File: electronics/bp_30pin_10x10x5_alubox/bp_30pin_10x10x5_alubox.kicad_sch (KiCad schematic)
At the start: 2 parts

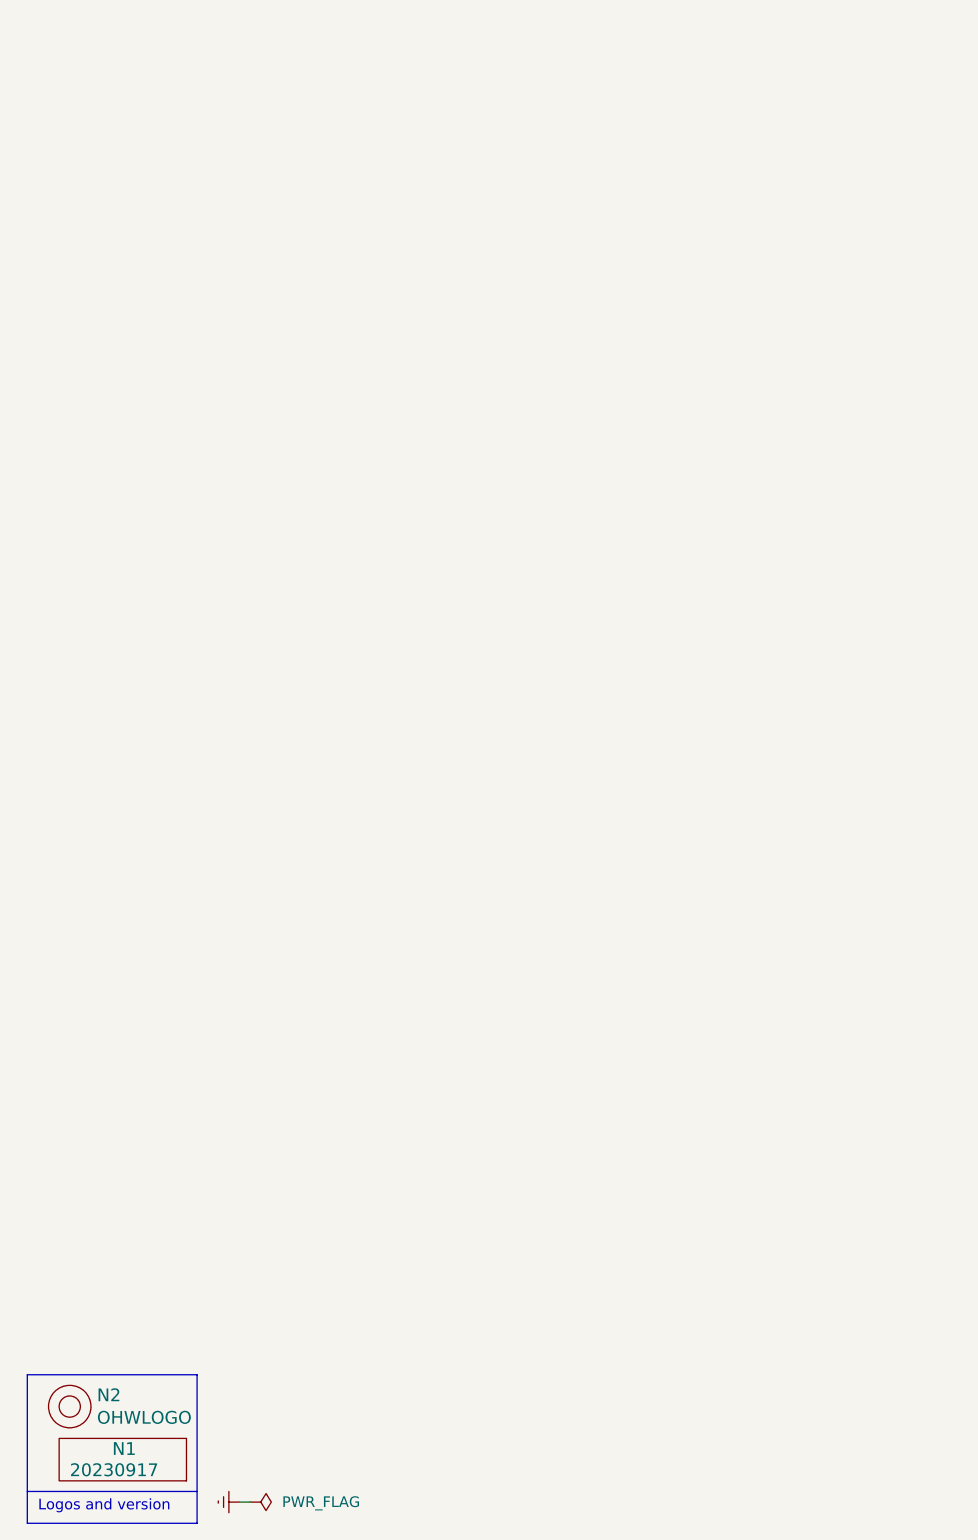
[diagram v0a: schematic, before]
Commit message: added lock files to gitignore, WIP 30 pin backplane
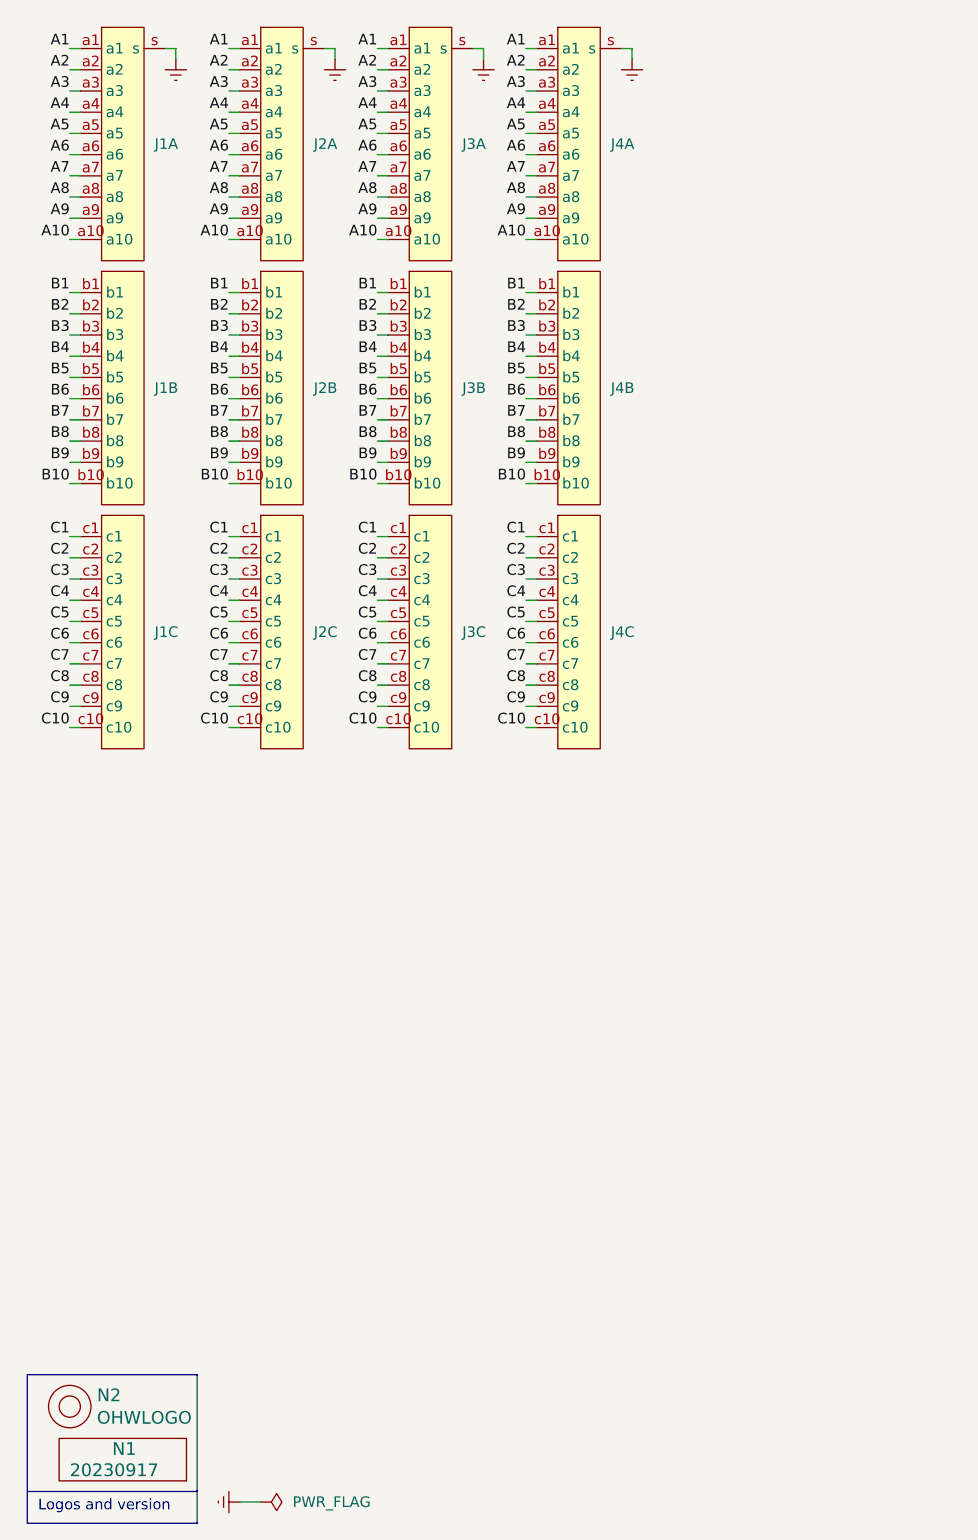
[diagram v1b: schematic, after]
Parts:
- added J1, J2, J3, J4: ~, SquantorConnectors:DIN41612_C3_3x10_Female_Vertical_THT_shields, symbol SquantorConnectors:DIN41612_03x10_ABC_screws
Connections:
- net Earth: now also J1.s, J2.s, J3.s, J4.s
- new net A1: J1.a1, J2.a1, J3.a1, J4.a1
- new net A10: J1.a10, J2.a10, J3.a10, J4.a10
- new net A2: J1.a2, J2.a2, J3.a2, J4.a2
- new net A3: J1.a3, J2.a3, J3.a3, J4.a3
- new net A4: J1.a4, J2.a4, J3.a4, J4.a4
- new net A5: J1.a5, J2.a5, J3.a5, J4.a5
- new net A6: J1.a6, J2.a6, J3.a6, J4.a6
- new net A7: J1.a7, J2.a7, J3.a7, J4.a7
- new net A8: J1.a8, J2.a8, J3.a8, J4.a8
- new net A9: J1.a9, J2.a9, J3.a9, J4.a9
- new net B1: J1.b1, J2.b1, J3.b1, J4.b1
- new net B10: J1.b10, J2.b10, J3.b10, J4.b10
- new net B2: J1.b2, J2.b2, J3.b2, J4.b2
- new net B3: J1.b3, J2.b3, J3.b3, J4.b3
- new net B4: J1.b4, J2.b4, J3.b4, J4.b4
- new net B5: J1.b5, J2.b5, J3.b5, J4.b5
- new net B6: J1.b6, J2.b6, J3.b6, J4.b6
- new net B7: J1.b7, J2.b7, J3.b7, J4.b7
- new net B8: J1.b8, J2.b8, J3.b8, J4.b8
- new net B9: J1.b9, J2.b9, J3.b9, J4.b9
- new net C1: J1.c1, J2.c1, J3.c1, J4.c1
- new net C10: J1.c10, J2.c10, J3.c10, J4.c10
- new net C2: J1.c2, J2.c2, J3.c2, J4.c2
- new net C3: J1.c3, J2.c3, J3.c3, J4.c3
- new net C4: J1.c4, J2.c4, J3.c4, J4.c4
- new net C5: J1.c5, J2.c5, J3.c5, J4.c5
- new net C6: J1.c6, J2.c6, J3.c6, J4.c6
- new net C7: J1.c7, J2.c7, J3.c7, J4.c7
- new net C8: J1.c8, J2.c8, J3.c8, J4.c8
- new net C9: J1.c9, J2.c9, J3.c9, J4.c9

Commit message: Place and route done
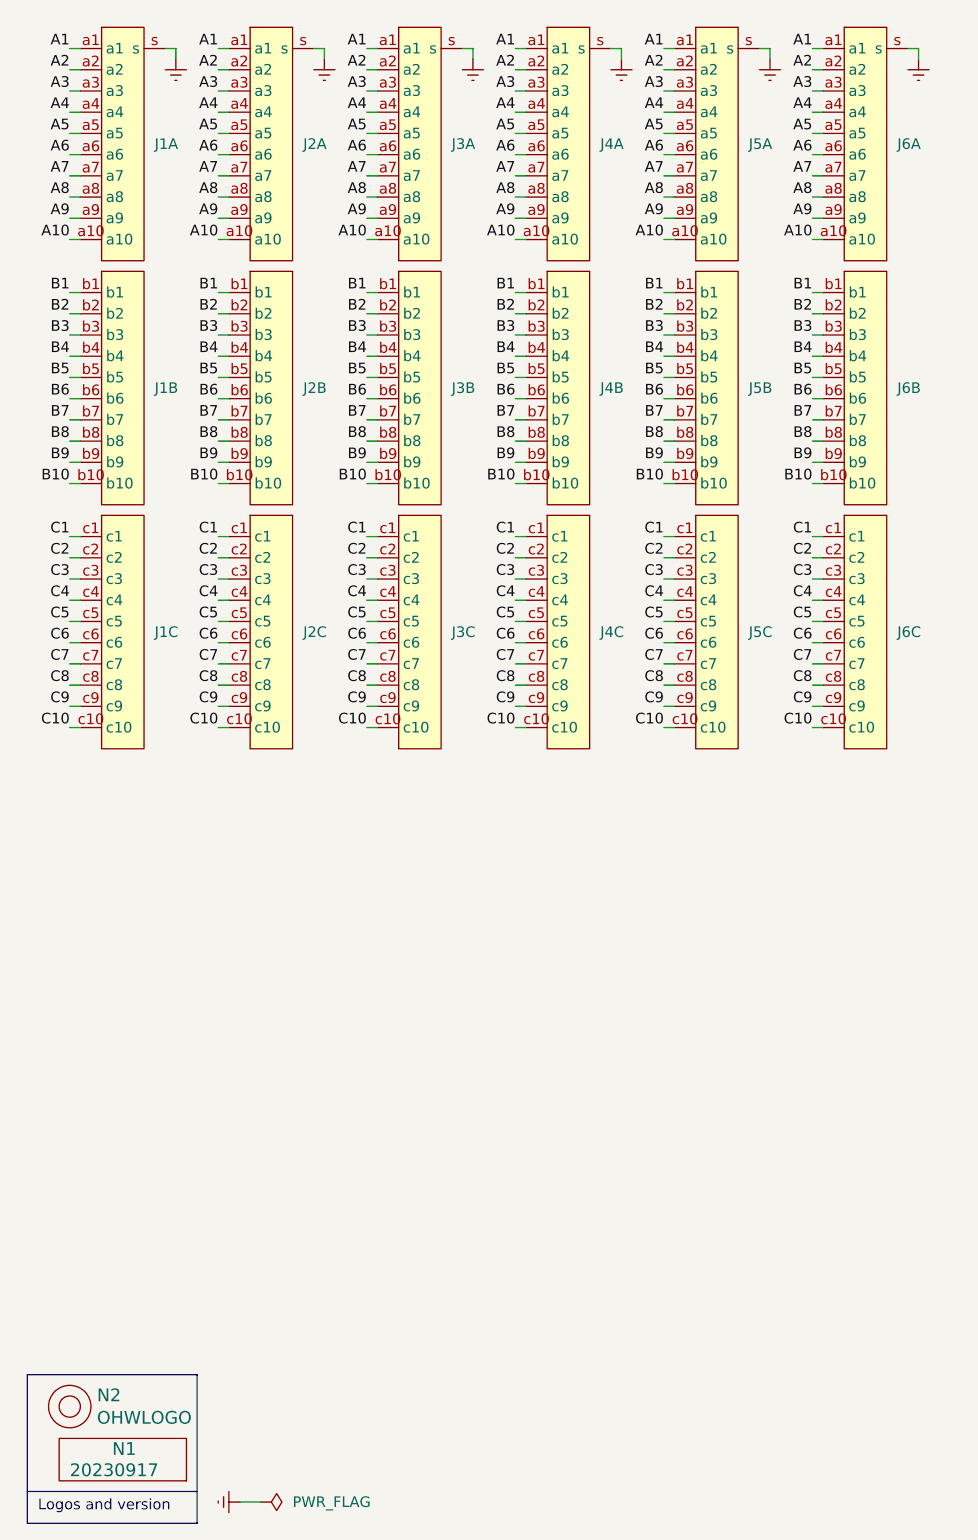
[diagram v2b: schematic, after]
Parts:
- added J5, J6: ~, SquantorConnectors:DIN41612_R3_3x10_Male_Vertical_THT_shield, symbol SquantorConnectors:DIN41612_03x10_ABC_screws
- J1, J2, J3, J4: footprint SquantorConnectors:DIN41612_C3_3x10_Female_Vertical_THT_shields -> SquantorConnectors:DIN41612_R3_3x10_Male_Vertical_THT_shield
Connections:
- net A1: now also J5.a1, J6.a1
- net A10: now also J5.a10, J6.a10
- net A2: now also J5.a2, J6.a2
- net A3: now also J5.a3, J6.a3
- net A4: now also J5.a4, J6.a4
- net A5: now also J5.a5, J6.a5
- net A6: now also J5.a6, J6.a6
- net A7: now also J5.a7, J6.a7
- net A8: now also J5.a8, J6.a8
- net A9: now also J5.a9, J6.a9
- net B1: now also J5.b1, J6.b1
- net B10: now also J5.b10, J6.b10
- net B2: now also J5.b2, J6.b2
- net B3: now also J5.b3, J6.b3
- net B4: now also J5.b4, J6.b4
- net B5: now also J5.b5, J6.b5
- net B6: now also J5.b6, J6.b6
- net B7: now also J5.b7, J6.b7
- net B8: now also J5.b8, J6.b8
- net B9: now also J5.b9, J6.b9
- net C1: now also J5.c1, J6.c1
- net C10: now also J5.c10, J6.c10
- net C2: now also J5.c2, J6.c2
- net C3: now also J5.c3, J6.c3
- net C4: now also J5.c4, J6.c4
- net C5: now also J5.c5, J6.c5
- net C6: now also J5.c6, J6.c6
- net C7: now also J5.c7, J6.c7
- net C8: now also J5.c8, J6.c8
- net C9: now also J5.c9, J6.c9
- net Earth: now also J5.s, J6.s
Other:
- moved on the sheet: J2A, J2B, J2C, J3A, J3B, J3C, J4A, J4B, J4C

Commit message: updated versionnumber, added block for backplane, larger copper plane spacing
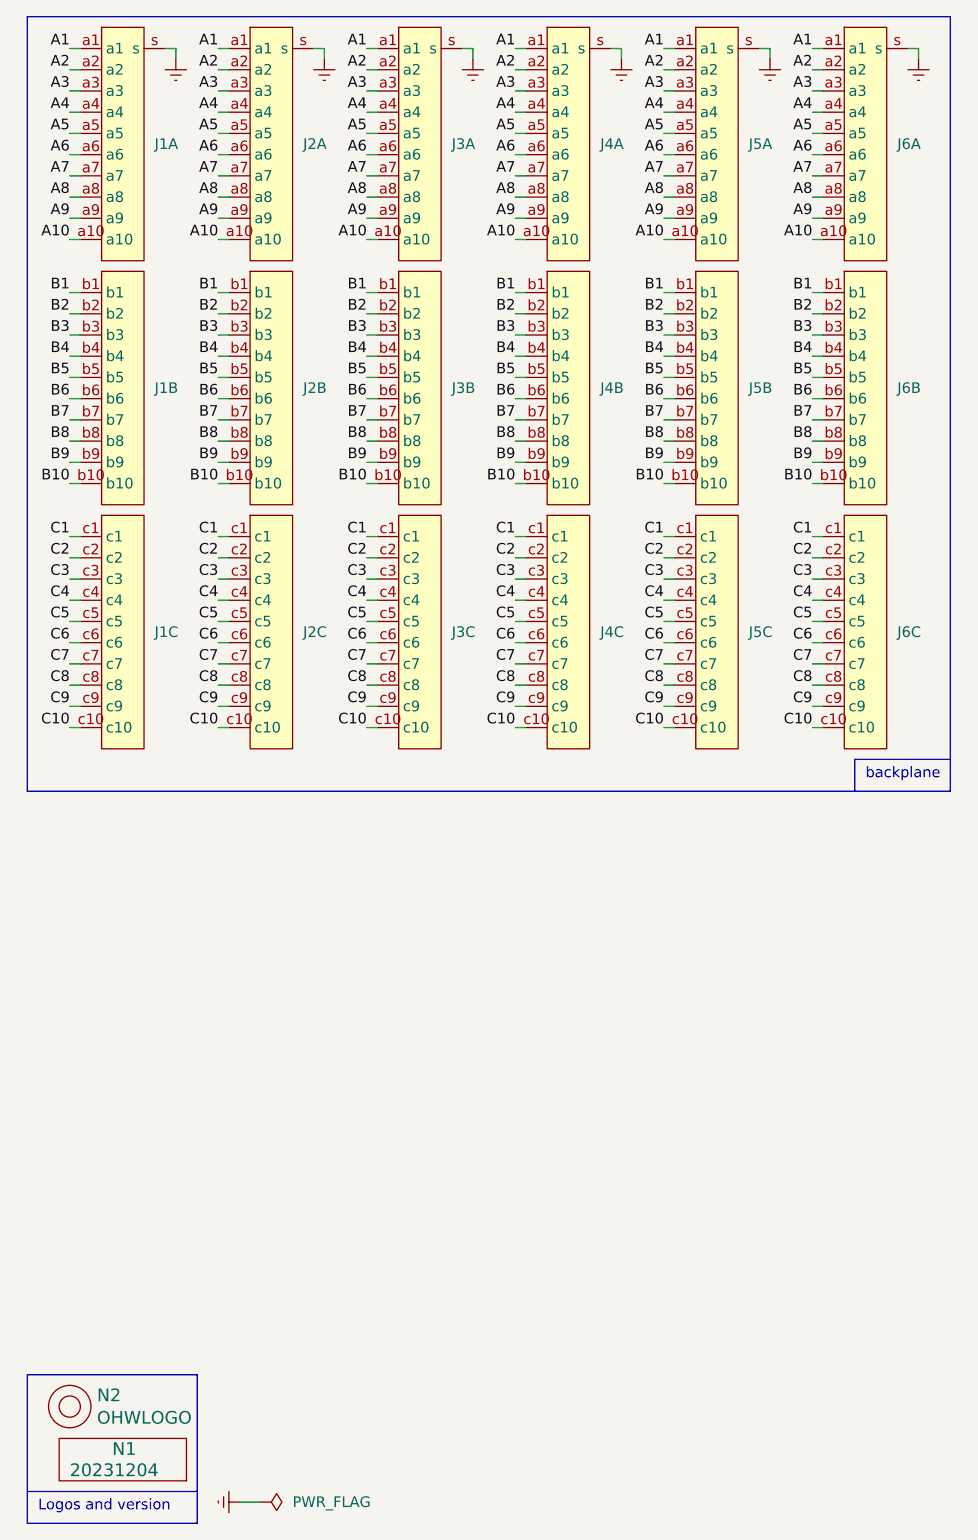
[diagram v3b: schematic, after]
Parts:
- N1: value 20230917 -> 20231204
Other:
- note added: "backplane"
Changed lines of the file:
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@@
+    (stroke (width 0) (type default))
+  )
+  (polyline (pts (xy 15.24 15.24) (xy 125.73 15.24))
     (stroke (width 0) (type default))
   )
@@
     (stroke (width 0) (type default))
   )
+  (polyline (pts (xy 125.73 104.14) (xy 114.3 104.14))
+    (stroke (width 0) (type default))
+  )
   (wire (pts (xy 55.88 66.04) (xy 57.15 66.04))
     (stroke (width 0) (type default))
@@
     (stroke (width 0) (type default))
   )
+  (polyline (pts (xy 114.3 104.14) (xy 114.3 107.95))
+    (stroke (width 0) (type default))
+  )
   (wire (pts (xy 38.1 68.58) (xy 39.37 68.58))
     (stroke (width 0) (type default))
@@
     (stroke (width 0) (type default))
   )
+  (polyline (pts (xy 125.73 15.24) (xy 125.73 107.95))
+    (stroke (width 0) (type default))
+  )
   (wire (pts (xy 20.32 58.42) (xy 21.59 58.42))
     (stroke (width 0) (type default))
@@
     (stroke (width 0) (type default))
   )
+  (polyline (pts (xy 15.24 15.24) (xy 15.24 107.95))
+    (stroke (width 0) (type default))
+  )
   (wire (pts (xy 73.66 21.59) (xy 74.93 21.59))
     (stroke (width 0) (type default))
@@
     (stroke (width 0) (type default))
   )
+  (polyline (pts (xy 125.73 107.95) (xy 15.24 107.95))
+    (stroke (width 0) (type default))
+  )
   (polyline (pts (xy 15.24 195.58) (xy 35.56 195.58))
     (stroke (width 0) (type default))
@@
   )
   (text "Logos and version" (at 16.51 194.31 0)
+    (effects (font (size 1.27 1.27)) (justify left bottom))
+  )
+  (text "backplane" (at 115.57 106.68 0)
     (effects (font (size 1.27 1.27)) (justify left bottom))
   )
@@
       (effects (font (size 1.524 1.524)) (justify left))
     )
-    (property "Value" "20230917" (at 20.32 189.23 0)
+    (property "Value" "20231204" (at 20.32 189.23 0)
       (effects (font (size 1.524 1.524)) (justify left))
     )

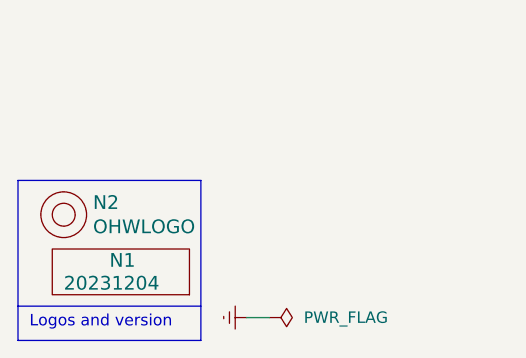
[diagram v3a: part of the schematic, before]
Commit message: updated board to Aisler Budget design rules, fixed DRC errors
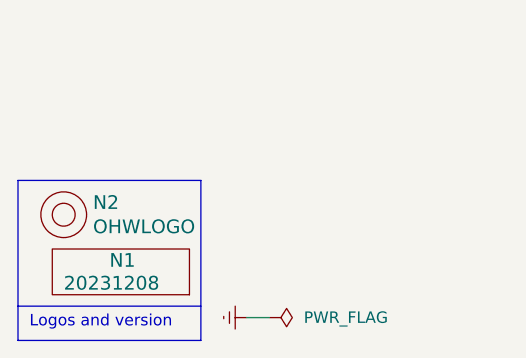
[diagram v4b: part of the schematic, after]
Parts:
- N1: value 20231204 -> 20231208
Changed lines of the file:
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@@
       (effects (font (size 1.524 1.524)) (justify left))
     )
-    (property "Value" "20231204" (at 20.32 189.23 0)
+    (property "Value" "20231208" (at 20.32 189.23 0)
       (effects (font (size 1.524 1.524)) (justify left))
     )
